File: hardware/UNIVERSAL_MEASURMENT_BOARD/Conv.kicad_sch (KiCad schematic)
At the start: 99 parts, among them U10 TPS54202HDDCR, U12 TPS54202HDDCR, U13 L7805ABD2T-TR, U15 TLV76133KVUR, U16 TLV76133KVUR, U2 LT3471EDD#PBF, U3 MAX6063AEUR+T, U5 ISL21010CFH315Z-TK, U7 L7812ABD2T-TR, U8 MC7815BDTRKG, U9 MC79M15CDTRKG

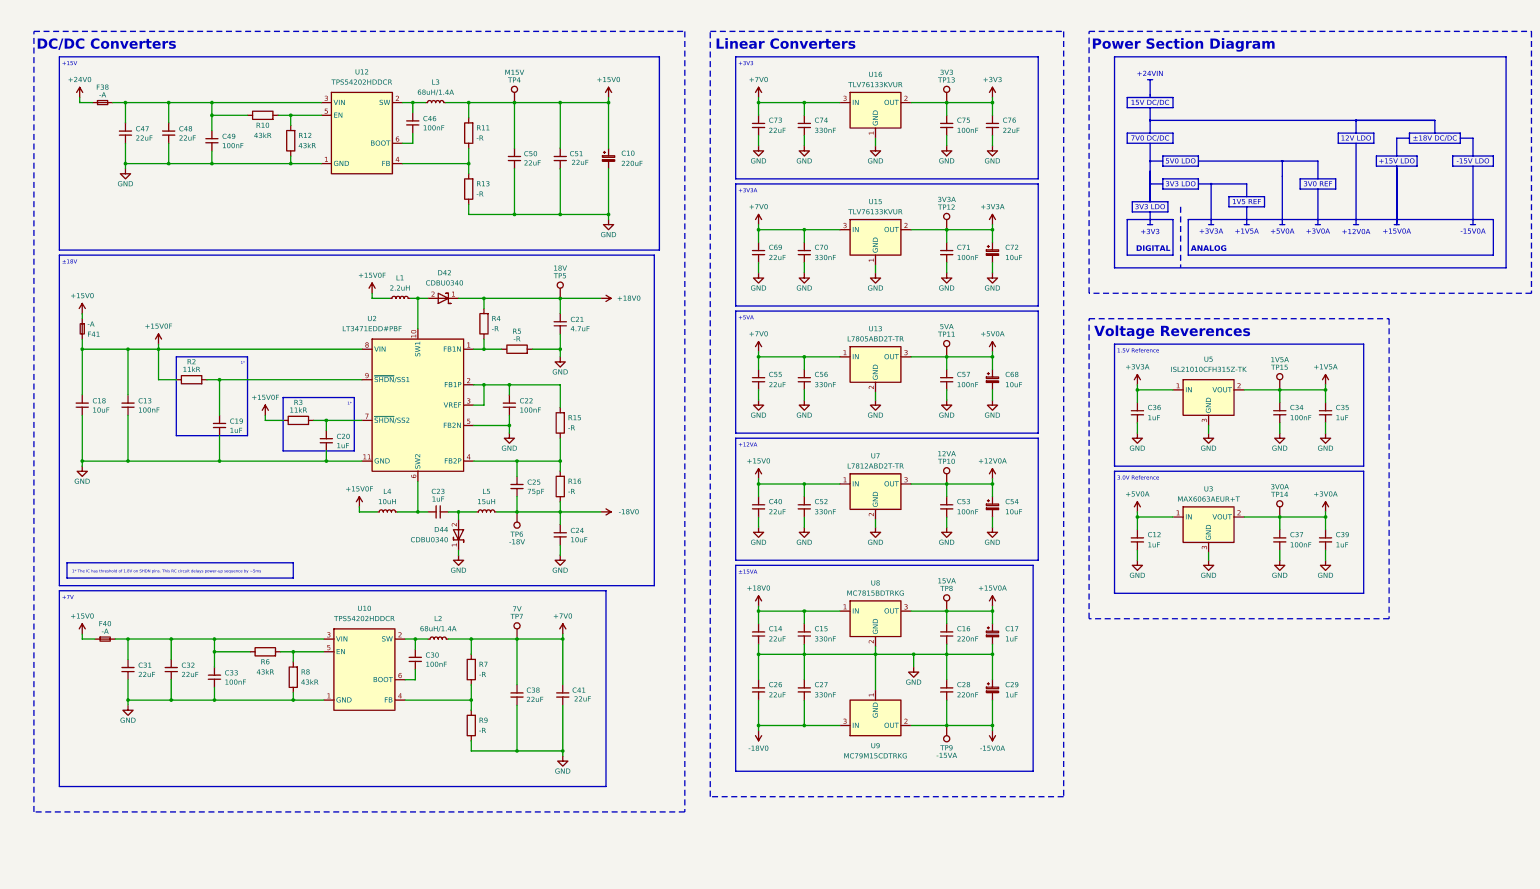
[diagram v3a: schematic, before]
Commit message: added footprints
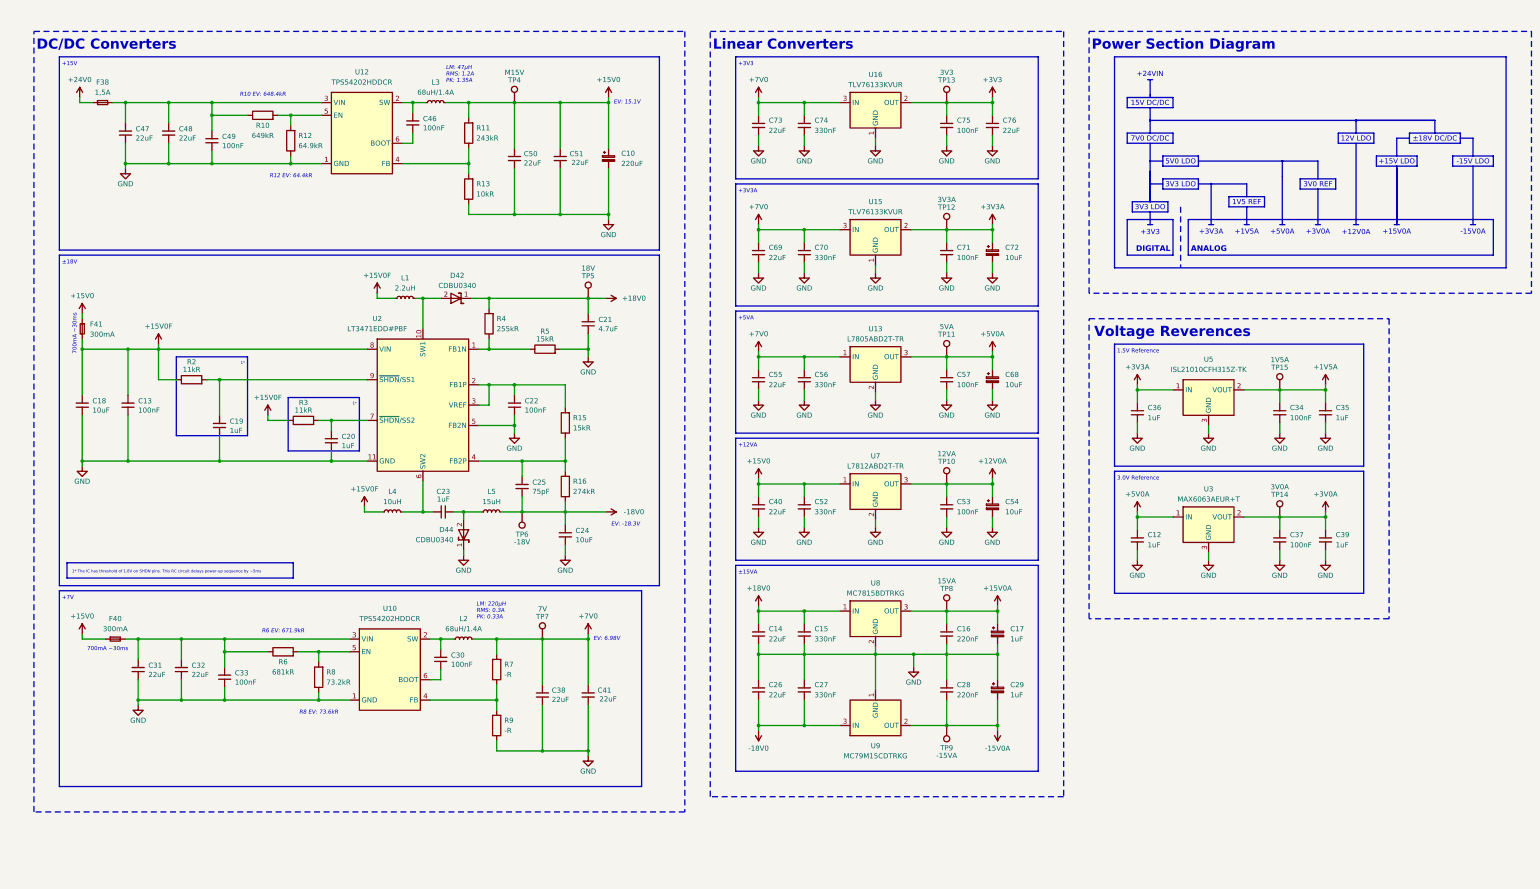
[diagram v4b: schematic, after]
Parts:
- C10: footprint (none) -> Capacitor_SMD:C_0805_2012Metric
- C12, C14, C15, C16, C19, C20, C22, C23, C25, C26, C27, C28, C31, C32, C34, C35, C36, C37, C38, C39, C40, C41, C52, C53, C55, C56, C57, C69, C70, C71, C73, C74, C75, C76: footprint Capacitor_SMD:C_0805_2012Metric -> Capacitor_SMD:C_0603_1608Metric
- C17, C29, C54, C68, C72: footprint (none) -> Capacitor_SMD:C_0603_1608Metric
- D42, D44: footprint DIOM179X85N -> Diode_SMD:D_0603_1608Metric
- F38: value -A -> 1,5A; footprint (none) -> Resistor_SMD:R_0805_2012Metric
- F40, F41: value -A -> 300mA; footprint (none) -> Resistor_SMD:R_0603_1608Metric
- R10: value 43kR -> 649kR; footprint (none) -> Resistor_SMD:R_0603_1608Metric
- R11: value -R -> 243kR; footprint (none) -> Resistor_SMD:R_0603_1608Metric
- R12: value 43kR -> 64.9kR; footprint (none) -> Resistor_SMD:R_0603_1608Metric
- R13: value -R -> 10kR; footprint (none) -> Resistor_SMD:R_0603_1608Metric
- R15, R5: value -R -> 15kR; footprint (none) -> Resistor_SMD:R_0603_1608Metric
- R16: value -R -> 274kR; footprint (none) -> Resistor_SMD:R_0603_1608Metric
- R2, R3, R7, R9: footprint (none) -> Resistor_SMD:R_0603_1608Metric
- R4: value -R -> 255kR; footprint (none) -> Resistor_SMD:R_0603_1608Metric
- R6: value 43kR -> 681kR; footprint (none) -> Resistor_SMD:R_0603_1608Metric
- R8: value 43kR -> 73.2kR; footprint (none) -> Resistor_SMD:R_0603_1608Metric
- TP10, TP11, TP12, TP13, TP14, TP15, TP4, TP5, TP6, TP7, TP8, TP9: footprint (none) -> TestPoint:TestPoint_Pad_D1.5mm
- U9: footprint DPAK_(SINGLE-GAUGE)_TO-252(369C)_ISSUE_F -> MC79M15CDTRKG:DPAK__SINGLE-GAUGE__TO-252_369C__ISSUE_F
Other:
- note added: "700mA ~30ms"
- note added: "EV: -18.3V"
- note added: "EV: 15.1V"
- note added: "EV: 6.98V"
- note added: "LM: 220µH RMS: 0.3A PK: 0.33A"
- note added: "LM: 47µH RMS: 1.2A PK: 1.35A"
- note added: "R10 EV: 648.4kR"
- note added: "R12 EV: 64.4kR"
- note added: "R6 EV: 671.9kR"
- note added: "R8 EV: 73.6kR"
- company: PUT Motorsport Formula Student team -> PUT Motorsport Formula Student Team
- moved on the sheet: C17, C20, C21, C22, C23, C24, C25, C29, C30, C31, C32, C33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

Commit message: first outcom of pcb design
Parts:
- removed L1: 2.2uH, Inductor_SMD:L_TDK_VLS6045EX_VLS6045AF, symbol Samacsys_kicad_sym:SRR4028-271Y
- removed L2, L3: 68uH/1.4A, Inductor_SMD:L_TDK_VLS6045EX_VLS6045AF, symbol Samacsys_kicad_sym:SRR4028-271Y
- removed L4: 10uH, Inductor_SMD:L_TDK_VLS6045EX_VLS6045AF, symbol Samacsys_kicad_sym:SRR4028-271Y
- removed L5: 15uH, Inductor_SMD:L_TDK_VLS6045EX_VLS6045AF, symbol Samacsys_kicad_sym:SRR4028-271Y
- removed U15, U16: TLV76133KVUR, TLV76133KVUR, symbol TLV76133KVUR:TLV76133KVUR
- removed U3: MAX6063AEUR+T, SOT95P229X119-3N, symbol MAX6063AEUR+T:MAX6063AEUR+T
- removed U8: MC7815BDTRKG, NVD5117PLT4GVF01, symbol MC7815BDTRKG:MC7815BDTRKG
- removed U9: MC79M15CDTRKG, MC79M15CDTRKG:DPAK__SINGLE-GAUGE__TO-252_369C__ISSUE_F, symbol MC79M15CDTRKG:MC79M15CDTRKG
- added C34: 22uF, REST:C_0603_1608Metric, symbol Device:C_Small
- added L1: PM3604-5-RC, PM3604-5-RC:PM3604-5-RC, symbol PM3604-5-RC:PM3604-5-RC
- added L2: 74408943100, 74408943100:WE-SPC_48XX78, symbol 74408943100:74408943100
- added L3: 74437349560, 74437349560, symbol 74437349560:74437349560
- added L6: ASPIAIG-S8050-221M-T, ASPIAIG-S8050-221M-T:INDPM8080X520N, symbol ASPIAIG-S8050-221M-T:ASPIAIG-S8050-221M-T
- added U12: L78L15ACD13TR, SOIC127P600X175-8N, symbol L78L15ACD13TR:L78L15ACD13TR
- added U13: L79L15ACD13TR, SOIC127P600X175-8N, symbol L79L15ACD13TR:L79L15ACD13TR
- added U15: ISL21010CFH330Z-TK, SOT95P237X112-3N, symbol ISL21010CFH330Z-TK:ISL21010CFH330Z-TK
- added U8, U9: UA78M33CDCYRG3, SOT230P700X180-4N, symbol UA78M33CDCYRG3:UA78M33CDCYRG3
- C12: renamed from C18; footprint Capacitor_SMD:C_0805_2012Metric -> REST:C_0805_2012Metric
- C13: renamed from C47; footprint Capacitor_SMD:C_0805_2012Metric -> REST:C_0805_2012Metric
- C14: renamed from C13; footprint Capacitor_SMD:C_0805_2012Metric -> REST:C_0603_1608Metric
- C15: renamed from C31; footprint Capacitor_SMD:C_0603_1608Metric -> REST:C_0603_1608Metric
- C16: renamed from C48; footprint Capacitor_SMD:C_0805_2012Metric -> REST:C_0805_2012Metric
- C17: renamed from C32; footprint Capacitor_SMD:C_0603_1608Metric -> REST:C_0603_1608Metric
- C18: renamed from C49; footprint Capacitor_SMD:C_0603_1608Metric -> REST:C_0603_1608Metric
- C19: footprint Capacitor_SMD:C_0603_1608Metric -> REST:C_0603_1608Metric
- C20: renamed from C33; footprint Capacitor_SMD:C_0603_1608Metric -> REST:C_0603_1608Metric
- C21: renamed from C20; footprint Capacitor_SMD:C_0603_1608Metric -> REST:C_0603_1608Metric
- C22: renamed from C46; footprint Capacitor_SMD:C_0603_1608Metric -> REST:C_0603_1608Metric
- C23: renamed from C30; footprint Capacitor_SMD:C_0603_1608Metric -> REST:C_0603_1608Metric
- C24: renamed from C23; footprint Capacitor_SMD:C_0603_1608Metric -> REST:C_0805_2012Metric
- C25: renamed from C50; footprint Capacitor_SMD:C_0805_2012Metric -> REST:C_0805_2012Metric
- C26: renamed from C22; footprint Capacitor_SMD:C_0603_1608Metric -> REST:C_0603_1608Metric
- C27: renamed from C25; footprint Capacitor_SMD:C_0603_1608Metric -> REST:C_0603_1608Metric
- C28: renamed from C38; value 22uF -> 100nF; footprint Capacitor_SMD:C_0603_1608Metric -> REST:C_0603_1608Metric
- C29: renamed from C51; footprint Capacitor_SMD:C_0805_2012Metric -> REST:C_0805_2012Metric
- C30: renamed from C24; footprint Capacitor_SMD:C_0805_2012Metric -> REST:C_0805_2012Metric
- C31: renamed from C21; footprint Capacitor_SMD:C_0805_2012Metric -> REST:C_0805_2012Metric
- C32: renamed from C41; footprint Capacitor_SMD:C_0603_1608Metric -> REST:C_0603_1608Metric
- C33: renamed from C10; footprint Capacitor_SMD:C_0805_2012Metric -> REST:CP_Elec_8x10
- C35: renamed from C73; footprint Capacitor_SMD:C_0603_1608Metric -> REST:C_0603_1608Metric
- C36: renamed from C69; footprint Capacitor_SMD:C_0603_1608Metric -> REST:C_0603_1608Metric
- C37: renamed from C55; footprint Capacitor_SMD:C_0603_1608Metric -> REST:C_0603_1608Metric
- C38: renamed from C40; footprint Capacitor_SMD:C_0603_1608Metric -> REST:C_0603_1608Metric
- C39: renamed from C14; footprint Capacitor_SMD:C_0603_1608Metric -> REST:C_0603_1608Metric
- C40: renamed from C26; footprint Capacitor_SMD:C_0603_1608Metric -> REST:C_0603_1608Metric
- C41: renamed from C74; footprint Capacitor_SMD:C_0603_1608Metric -> REST:C_0603_1608Metric
- C42: renamed from C70; footprint Capacitor_SMD:C_0603_1608Metric -> REST:C_0603_1608Metric
- C43: renamed from C56; footprint Capacitor_SMD:C_0603_1608Metric -> REST:C_0603_1608Metric
- C44: renamed from C52; footprint Capacitor_SMD:C_0603_1608Metric -> REST:C_0603_1608Metric
- C45: renamed from C15; footprint Capacitor_SMD:C_0603_1608Metric -> REST:C_0603_1608Metric
- C46: renamed from C27; footprint Capacitor_SMD:C_0603_1608Metric -> REST:C_0603_1608Metric
- C47: renamed from C75; footprint Capacitor_SMD:C_0603_1608Metric -> REST:C_0603_1608Metric
- C48: renamed from C71; footprint Capacitor_SMD:C_0603_1608Metric -> REST:C_0603_1608Metric
- C49: renamed from C57; footprint Capacitor_SMD:C_0603_1608Metric -> REST:C_0603_1608Metric
- C50: renamed from C53; footprint Capacitor_SMD:C_0603_1608Metric -> REST:C_0603_1608Metric
- C51: renamed from C16; footprint Capacitor_SMD:C_0603_1608Metric -> REST:C_0603_1608Metric
- C52: renamed from C28; footprint Capacitor_SMD:C_0603_1608Metric -> REST:C_0603_1608Metric
- C53: renamed from C76; footprint Capacitor_SMD:C_0603_1608Metric -> REST:C_0603_1608Metric
- C54: renamed from C72; footprint Capacitor_SMD:C_0603_1608Metric -> REST:CP_Elec_4x5.8
- C55: renamed from C68; footprint Capacitor_SMD:C_0603_1608Metric -> REST:CP_Elec_4x5.8
- C56: renamed from C54; footprint Capacitor_SMD:C_0603_1608Metric -> REST:CP_Elec_4x5.8
- C57: renamed from C17; footprint Capacitor_SMD:C_0603_1608Metric -> REST:CP_Elec_4x5.4
- C58: renamed from C29; footprint Capacitor_SMD:C_0603_1608Metric -> REST:CP_Elec_4x5.4
- C59: renamed from C36; footprint Capacitor_SMD:C_0603_1608Metric -> REST:C_0603_1608Metric
- C60: renamed from C12; footprint Capacitor_SMD:C_0603_1608Metric -> REST:C_0603_1608Metric
- C61: renamed from C34; footprint Capacitor_SMD:C_0603_1608Metric -> REST:C_0603_1608Metric
- C62: renamed from C37; footprint Capacitor_SMD:C_0603_1608Metric -> REST:C_0603_1608Metric
- C63: renamed from C35; footprint Capacitor_SMD:C_0603_1608Metric -> REST:C_0603_1608Metric
- C64: renamed from C39; footprint Capacitor_SMD:C_0603_1608Metric -> REST:C_0603_1608Metric
- D1: renamed from D42; footprint Diode_SMD:D_0603_1608Metric -> REST:D_0603_1608Metric
- D2: renamed from D44; footprint Diode_SMD:D_0603_1608Metric -> REST:D_0603_1608Metric
- F1: renamed from F41; footprint Resistor_SMD:R_0603_1608Metric -> REST:F_0603_1608Metric
- F2: renamed from F38; footprint Resistor_SMD:R_0805_2012Metric -> REST:F_0805_2012Metric
- F3: renamed from F40; footprint Resistor_SMD:R_0603_1608Metric -> REST:F_0603_1608Metric
- R10: renamed from R8; footprint Resistor_SMD:R_0603_1608Metric -> REST:R_0603_1608Metric
- R11: footprint Resistor_SMD:R_0603_1608Metric -> REST:R_0603_1608Metric
- R12: renamed from R13; footprint Resistor_SMD:R_0603_1608Metric -> REST:R_0603_1608Metric
- R13: renamed from R4; footprint Resistor_SMD:R_0603_1608Metric -> REST:R_0603_1608Metric
- R14: renamed from R7; footprint Resistor_SMD:R_0603_1608Metric -> REST:R_0603_1608Metric
- R15: renamed from R9; footprint Resistor_SMD:R_0603_1608Metric -> REST:R_0603_1608Metric
- R16: renamed from R5; footprint Resistor_SMD:R_0603_1608Metric -> REST:R_0603_1608Metric
- R17: renamed from R15; footprint Resistor_SMD:R_0603_1608Metric -> REST:R_0603_1608Metric
- R18: renamed from R16; footprint Resistor_SMD:R_0603_1608Metric -> REST:R_0603_1608Metric
- R5: renamed from R2; footprint Resistor_SMD:R_0603_1608Metric -> REST:R_0603_1608Metric
- R6: renamed from R10; footprint Resistor_SMD:R_0603_1608Metric -> REST:R_0603_1608Metric
- R7: renamed from R6; footprint Resistor_SMD:R_0603_1608Metric -> REST:R_0603_1608Metric
- R8: renamed from R12; footprint Resistor_SMD:R_0603_1608Metric -> REST:R_0603_1608Metric
- R9: renamed from R3; footprint Resistor_SMD:R_0603_1608Metric -> REST:R_0603_1608Metric
- TP1: renamed from TP4; footprint TestPoint:TestPoint_Pad_D1.5mm -> REST:TestPoint_Pad_D1.5mm
- TP10: renamed from TP9; footprint TestPoint:TestPoint_Pad_D1.5mm -> REST:TestPoint_Pad_D1.5mm
- TP11: renamed from TP15; footprint TestPoint:TestPoint_Pad_D1.5mm -> REST:TestPoint_Pad_D1.5mm
- TP12: renamed from TP14; footprint TestPoint:TestPoint_Pad_D1.5mm -> REST:TestPoint_Pad_D1.5mm
- TP2: renamed from TP6; footprint TestPoint:TestPoint_Pad_D1.5mm -> REST:TestPoint_Pad_D1.5mm
- TP3: renamed from TP7; footprint TestPoint:TestPoint_Pad_D1.5mm -> REST:TestPoint_Pad_D1.5mm
- TP4: renamed from TP5; footprint TestPoint:TestPoint_Pad_D1.5mm -> REST:TestPoint_Pad_D1.5mm
- TP5: renamed from TP13; footprint TestPoint:TestPoint_Pad_D1.5mm -> REST:TestPoint_Pad_D1.5mm
- TP6: renamed from TP12; footprint TestPoint:TestPoint_Pad_D1.5mm -> REST:TestPoint_Pad_D1.5mm
- TP7: renamed from TP11; footprint TestPoint:TestPoint_Pad_D1.5mm -> REST:TestPoint_Pad_D1.5mm
- TP8: renamed from TP10; footprint TestPoint:TestPoint_Pad_D1.5mm -> REST:TestPoint_Pad_D1.5mm
- TP9: renamed from TP8; footprint TestPoint:TestPoint_Pad_D1.5mm -> REST:TestPoint_Pad_D1.5mm
- renumbered U13 to U10, U7 to U11, U5 to U14, U12 to U5, U10 to U6, U2 to U7
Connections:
- net +15V0: now also L3.2
- net +15V0A: now also U12.1 (OUT)
- net +15V0F: now also L1.1, L2.1
- net +18V0: now also U12.8 (IN)
- net +3V0A: now also U15.2 (VOUT)
- net +3V3: now also U8.3 (OUT)
- net +3V3A: now also U9.3 (OUT)
- net +5V0A: now also U15.1 (IN)
- net +7V0: now also C34.1, L6.2, U8.1 (IN), U9.1 (IN)
- net -15V0A: now also U13.1 (OUT)
- net -18V0: now also L1.3, U13.2 (IN), U13.3 (VIN_2), U13.6 (VIN_3), U13.7 (VIN_4)
- net GND: now also C34.2, U12.2 (GND), U12.3 (GND_2), U12.6 (GND_3), U12.7 (GND_4), U13.5 (GND), U15.3 (GND), U8.2 (GND), U8.4 (GND), U9.2 (GND), U9.4 (GND)
- net at D1.2 (A), U7.10 (SW1): now also L2.2
- net at C23.2, U6.2 (SW): now also L6.1
- net at C24.2, U7.6 (SW2): now also L1.2
- net at C24.1, D2.2 (A): now also L1.4
- net at C22.2, U5.2 (SW): now also L3.1
- new net: U12.4 (NC_1), U12.5 (NC_2)

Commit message: Review fixes
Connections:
- net +15V0F: now also L1.2; no longer L1.1
- net at C24.2, U7.6 (SW2): now also L1.1; no longer L1.2
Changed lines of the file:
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@@
 		(lib_id "PM3604-5-RC:PM3604-5-RC")
 		(at 110.49 142.875 0)
+		(mirror y)
 		(unit 1)
 		(body_style 1)
@@
 		(in_pos_files yes)
 		(dnp no)
-		(fields_autoplaced yes)
 		(property "Reference" "L1"
-			(at 110.3812 137.795 0)
+			(at 110.5988 137.795 0)
 			(show_name no)
 			(do_not_autoplace no)
@@
 		)
 		(property "Value" "PM3604-5-RC"
-			(at 110.3812 140.335 0)
+			(at 110.5988 140.335 0)
 			(show_name no)
 			(do_not_autoplace no)
@@
 		)
 		(property "Footprint" "PM3604-5-RC:PM3604-5-RC"
-			(at 127 239.065 0)
+			(at 93.98 239.065 0)
 			(hide yes)
 			(show_name no)
@@
 		)
 		(property "Datasheet" "https://www.we-online.com/catalog/datasheet/74408943100.pdf"
-			(at 127 339.065 0)
+			(at 93.98 339.065 0)
 			(hide yes)
 			(show_name no)
@@
 		)
 		(property "Height" "3.3"
-			(at 127 539.065 0)
+			(at 93.98 539.065 0)
 			(hide yes)
 			(show_name no)
@@
 		)
 		(property "Mouser Part Number" "710-74408943100"
-			(at 127 639.065 0)
+			(at 93.98 639.065 0)
 			(hide yes)
 			(show_name no)
@@
 		)
 		(property "Mouser Price/Stock" "https://www.mouser.co.uk/ProductDetail/Wurth-Elektronik/74408943100?qs=iRra8H4EogoDYOxdhQi%252BEA%3D%3D"
-			(at 127 739.065 0)
+			(at 93.98 739.065 0)
 			(hide yes)
 			(show_name no)
@@
 		)
 		(property "Manufacturer_Name" "Wurth Elektronik"
-			(at 127 839.065 0)
+			(at 93.98 839.065 0)
 			(hide yes)
 			(show_name no)
@@
 		)
 		(property "Manufacturer_Part_Number" "74408943100"
-			(at 127 939.065 0)
+			(at 93.98 939.065 0)
 			(hide yes)
 			(show_name no)
